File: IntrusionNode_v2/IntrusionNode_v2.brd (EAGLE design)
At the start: 31 x 39.5 mm, 38 parts, among them IC1 MCP1703CB, Q1 MOSFET-PCHANNELSMD, U1 RFM69, U2 MCP73831, U3 ATMEGA328P-AU, U4 MMA8452Q, Y1 16MHZ

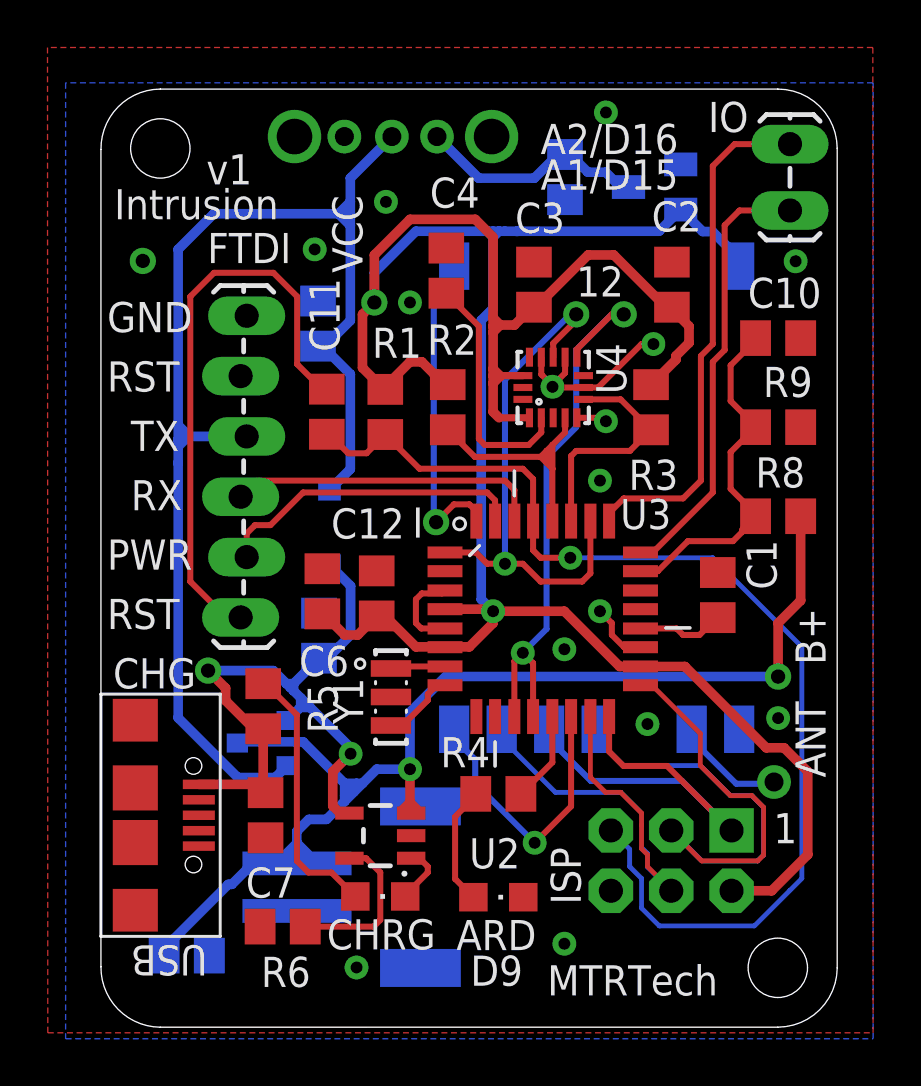
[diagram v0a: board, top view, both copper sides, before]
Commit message: *** Parts order place on Digikey
Web ID    149351856     Access ID    51215     Salesorder Number    43979223     Submitted    8/25/2015 4:06:46 PM

Modified board, adding notch, also changed part numbers for diode
and MOSFET to reduce current.
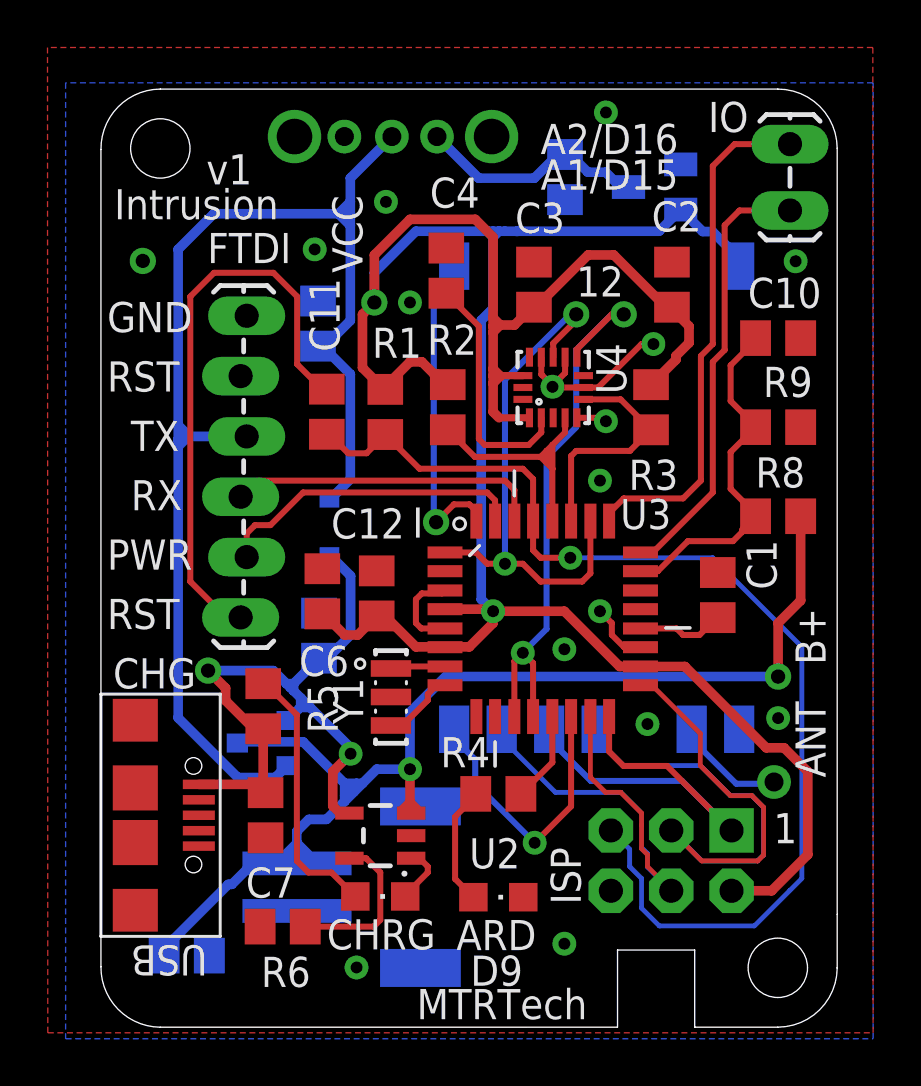
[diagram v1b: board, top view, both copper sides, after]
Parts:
- D1: value SCHOTTKY -> BAT20J; device SparkFun-DiscreteSemi:SOD-123 -> SparkFun-DiscreteSemi:SOD-323
- R7: value 10K -> 100K
- R8: value 3.3M -> 10M
- R9: value 5.36M -> 10M
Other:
- outline, holes or cut-outs redrawn
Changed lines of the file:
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@@
 <wire x1="0.00093125" y1="36.45415625" x2="-0.000040625" y2="2.043721875" width="0" layer="20"/>
 <wire x1="-0.000040625" y1="2.043721875" x2="2.500153125" y2="-0.500903125" width="0" layer="20" curve="90.00601"/>
-<wire x1="2.500153125" y1="-0.500903125" x2="28.500309375" y2="-0.498871875" width="0" layer="20"/>
+<wire x1="2.500153125" y1="-0.500903125" x2="21.75" y2="-0.5" width="0" layer="20"/>
+<wire x1="21.75" y1="-0.5" x2="21.75" y2="2.75" width="0" layer="20"/>
+<wire x1="21.75" y1="2.75" x2="25" y2="2.75" width="0" layer="20"/>
+<wire x1="25" y1="2.75" x2="25" y2="-0.498871875" width="0" layer="20"/>
+<wire x1="25" y1="-0.498871875" x2="28.500309375" y2="-0.498871875" width="0" layer="20"/>
 <wire x1="28.500309375" y1="-0.498871875" x2="31.0001125" y2="1.995940625" width="0" layer="20" curve="89.492188"/>
-<wire x1="31.0001125" y1="1.995940625" x2="30.999334375" y2="36.504784375" width="0" layer="20"/>
+<wire x1="31.0001125" y1="1.995940625" x2="31" y2="1.995940625" width="0" layer="20"/>
+<wire x1="31" y1="1.995940625" x2="31" y2="4.25" width="0" layer="20"/>
+<wire x1="31" y1="4.25" x2="30.999334375" y2="36.504784375" width="0" layer="20"/>
 <wire x1="30.999334375" y1="36.504784375" x2="28.4993" y2="38.999365625" width="0" layer="20" curve="89.9995"/>
 <wire x1="28.4993" y1="38.999365625" x2="2.5009" y2="38.9990125" width="0" layer="20"/>
@@
 <rectangle x1="21.2620375" y1="4.08928125" x2="21.7870375" y2="4.18928125" layer="42"/>
 <text x="29.3120375" y="8.51428125" size="1.27" layer="21" font="vector" ratio="10" rot="R180">1</text>
-<text x="18.7961375" y="0.83738125" size="1.27" layer="21" font="vector" ratio="10">MTRTech</text>
+<text x="13.2961375" y="-0.16261875" size="1.27" layer="21" font="vector" ratio="10">MTRTech</text>
 <rectangle x1="8.3620375" y1="18.56428125" x2="8.4620375" y2="19.06428125" layer="41"/>
 <hole x="28.5" y="2" drill="2.5"/>
@@
 </element>
 <element name="Q1" library="SparkFun-DiscreteSemi" package="SOT23-3" value="MOSFET-PCHANNELSMD" x="6.8420375" y="11.46428125" smashed="yes" rot="MR270">
-<attribute name="PARTNO" value="SSM3J328R,LF" x="6.8420375" y="11.46428125" size="1.778" layer="28" rot="MR270" display="off"/>
+<attribute name="PARTNO" value="PMV48XP,215" x="6.8420375" y="11.46428125" size="1.778" layer="28" rot="MR270" display="off"/>
 <attribute name="NAME" x="3.5265375" y="13.35628125" size="1.27" layer="26" font="vector" ratio="10" rot="MR180"/>
 <attribute name="VALUE" x="7.0325375" y="12.48028125" size="0.4064" layer="28" rot="MR270"/>
 </element>
-<element name="D1" library="SparkFun-DiscreteSemi" package="SOD-123" value="SCHOTTKY" x="9.6220375" y="20.54428125" smashed="yes" rot="MR270">
-<attribute name="PARTNO" value="B130LAW-7-F" x="9.6220375" y="20.54428125" size="1.778" layer="28" rot="MR270" display="off"/>
-<attribute name="NAME" x="10.1060375" y="25.16328125" size="1.27" layer="26" font="vector" ratio="10" rot="MR270"/>
-<attribute name="VALUE" x="11.0190375" y="21.56028125" size="0.4064" layer="28" rot="MR270"/>
-</element>
-<element name="R7" library="rcl" package="R0805" value="10K" x="9.1820375" y="15.98428125" smashed="yes" rot="MR270">
-<attribute name="PARTNO" value="RC2012J103CS" x="9.1820375" y="15.98428125" size="1.778" layer="28" rot="MR270" display="off"/>
+<element name="D1" library="SparkFun-DiscreteSemi" package="SOD-323" value="BAT20J" x="9.6220375" y="20.54428125" smashed="yes" rot="MR270">
+<attribute name="PARTNO" value="BAT20JFILM" x="9.6220375" y="20.54428125" size="1.778" layer="28" rot="MR270" display="off"/>
+<attribute name="NAME" x="11.8560375" y="22.16328125" size="1.27" layer="26" font="vector" ratio="10" rot="MR270"/>
+<attribute name="VALUE" value="BAT20J" x="11.0190375" y="21.56028125" size="0.4064" layer="28" rot="MR270"/>
+<attribute name="PROD_ID" value="DIO-11623" x="9.6220375" y="20.54428125" size="1.778" layer="28" rot="MR270" display="off"/>
+</element>
+<element name="R7" library="rcl" package="R0805" value="100K" x="9.1820375" y="15.98428125" smashed="yes" rot="MR270">
+<attribute name="PARTNO" value="RC2012J104CS" x="9.1820375" y="15.98428125" size="1.778" layer="28" rot="MR270" display="off"/>
 <attribute name="NAME" x="11.4720375" y="15.13928125" size="1.27" layer="26" font="vector" ratio="10" rot="MR270"/>
 <attribute name="VALUE" x="11.7220375" y="16.61928125" size="1.27" layer="28" rot="MR270"/>
@@
 <attribute name="VALUE" x="-4.8383625" y="11.68728125" size="1.27" layer="27" rot="R270"/>
 </element>
-<element name="R8" library="rcl" package="R0805" value="3.3M" x="28.5120375" y="21.01428125" smashed="yes" rot="R180">
-<attribute name="PARTNO" value="RC2012F335CS" x="28.5120375" y="21.01428125" size="1.778" layer="27" rot="R180" display="off"/>
+<element name="R8" library="rcl" package="R0805" value="10M" x="28.5120375" y="21.01428125" smashed="yes" rot="R180">
+<attribute name="PARTNO" value="RC2012F106CS" x="28.5120375" y="21.01428125" size="1.778" layer="27" rot="R180" display="off"/>
 <attribute name="NAME" x="29.6470375" y="23.49428125" size="1.27" layer="25" font="vector" ratio="10" rot="R180"/>
 <attribute name="VALUE" x="29.1470375" y="23.55428125" size="1.27" layer="27" rot="R180"/>
 </element>
-<element name="R9" library="rcl" package="R0805" value="5.36M" x="28.5120375" y="24.76428125" smashed="yes">
-<attribute name="PARTNO" value="RC2012F5364CS" x="28.5120375" y="24.76428125" size="1.778" layer="27" display="off"/>
+<element name="R9" library="rcl" package="R0805" value="10M" x="28.5120375" y="24.76428125" smashed="yes">
+<attribute name="PARTNO" value="RC2012F106CS" x="28.5120375" y="24.76428125" size="1.778" layer="27" display="off"/>
 <attribute name="NAME" x="27.8770375" y="26.03428125" size="1.27" layer="25" font="vector" ratio="10"/>
 <attribute name="VALUE" x="27.8770375" y="22.22428125" size="1.27" layer="27"/>
@@
 <via x="12" y="34.25" extent="1-16" drill="0.5"/>
 <via x="9" y="32.25" extent="1-16" drill="0.5"/>
+<wire x1="29.25" y1="31.75" x2="29.4620375" y2="28.51428125" width="0" layer="19" extent="1-1"/>
+<wire x1="9.3220375" y1="18.80428125" x2="9.1820375" y2="16.93428125" width="0" layer="19" extent="1-16"/>
+<wire x1="29.4620375" y1="24.76428125" x2="29.4620375" y2="28.51428125" width="0" layer="19" extent="1-1"/>
 </signal>
 <signal name="RST">
@@
 <wire x1="9.1420375" y1="28.17428125" x2="9.32571875" y2="28.17428125" width="0.4064" layer="16"/>
 <wire x1="9.32571875" y1="28.17428125" x2="10.5" y2="27" width="0.4064" layer="16"/>
-<wire x1="10.5" y1="27" x2="10.5" y2="22.99724375" width="0.4064" layer="16"/>
-<wire x1="10.5" y1="22.99724375" x2="9.6220375" y2="22.11928125" width="0.4064" layer="16"/>
 <wire x1="9.6120375" y1="28.26428125" x2="9.6120375" y2="28.3620375" width="0.4064" layer="16"/>
 <wire x1="9.6120375" y1="28.3620375" x2="10.5" y2="29.25" width="0.4064" layer="16"/>
@@
 <wire x1="10.5" y1="33.75" x2="10.5" y2="34.25" width="0.4064" layer="16"/>
 <wire x1="10.5" y1="34.25" x2="10.5" y2="35.25" width="0.4064" layer="16"/>
-<wire x1="3.25" y1="12.52631875" x2="3.25" y2="23.25" width="0.4064" layer="16"/>
+<wire x1="3.25" y1="12.52631875" x2="3.25" y2="23.95" width="0.4064" layer="16"/>
 <wire x1="3.25" y1="23.95" x2="3.25" y2="24.25" width="0.4064" layer="16"/>
 <wire x1="3.25" y1="24.25" x2="3.25" y2="24.85" width="0.4064" layer="16"/>
@@
 <wire x1="10" y1="33.75" x2="10.5" y2="33.25" width="0.4064" layer="16"/>
 <wire x1="3.25" y1="24.85" x2="3.7" y2="24.4" width="0.4064" layer="16"/>
-<wire x1="3.25" y1="23.25" x2="3.25" y2="23.95" width="0.4064" layer="16"/>
 <wire x1="3.25" y1="23.95" x2="3.7" y2="24.4" width="0.4064" layer="16"/>
+<wire x1="10.5" y1="27" x2="10.5" y2="22.57224375" width="0.4064" layer="16"/>
+<wire x1="10.5" y1="22.57224375" x2="9.6220375" y2="21.69428125" width="0.4064" layer="16"/>
 </signal>
 <signal name="N$4">
@@
 <wire x1="10.4619375" y1="8.51428125" x2="10.0620375" y2="8.51428125" width="0.4064" layer="1"/>
 <wire x1="10.0620375" y1="8.51428125" x2="9.7620375" y2="8.81428125" width="0.4064" layer="1"/>
-<wire x1="10.5120375" y1="16.01428125" x2="10.5120375" y2="18.07928125" width="0.4064" layer="16"/>
-<wire x1="10.5120375" y1="18.07928125" x2="9.6220375" y2="18.96928125" width="0.4064" layer="16"/>
 <wire x1="4.1220375" y1="9.72428125" x2="6.5820375" y2="9.72428125" width="0.4064" layer="1"/>
 <wire x1="6.5820375" y1="9.72428125" x2="6.9320375" y2="9.37428125" width="0.4064" layer="1"/>
@@
 <wire x1="5.25" y1="13.25" x2="6.43571875" y2="12.06428125" width="0.4064" layer="1"/>
 <wire x1="6.43571875" y1="12.06428125" x2="6.8320375" y2="12.06428125" width="0.4064" layer="1"/>
+<wire x1="10.5120375" y1="16.01428125" x2="10.5120375" y2="18.50428125" width="0.4064" layer="16"/>
+<wire x1="10.5120375" y1="18.50428125" x2="9.6220375" y2="19.39428125" width="0.4064" layer="16"/>
 </signal>
 <signal name="N$7">

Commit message: ** Place OSH Park Order Number Er6KsneG, project name IntrusionNode_v2_150827
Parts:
- moved R6 5.71 mm to (12.7, 1.17), turned to 0 degrees
- moved ARD 0.50 mm to (16.7, 4.47)
- moved CHRG 0.50 mm to (11.8, 4.50)
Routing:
- net N$7: track 2.50 -> 3.18 mm
- net N$5: track 5.03 -> 5.53 mm
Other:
- board text removed: "D9"
